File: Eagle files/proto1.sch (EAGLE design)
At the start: 10 parts, among them U1 RASPBERRY_PICOTH, U2 GY-521MPU6050, U3 HMC5883LGY-271, U4 ESP8266_ESP-01

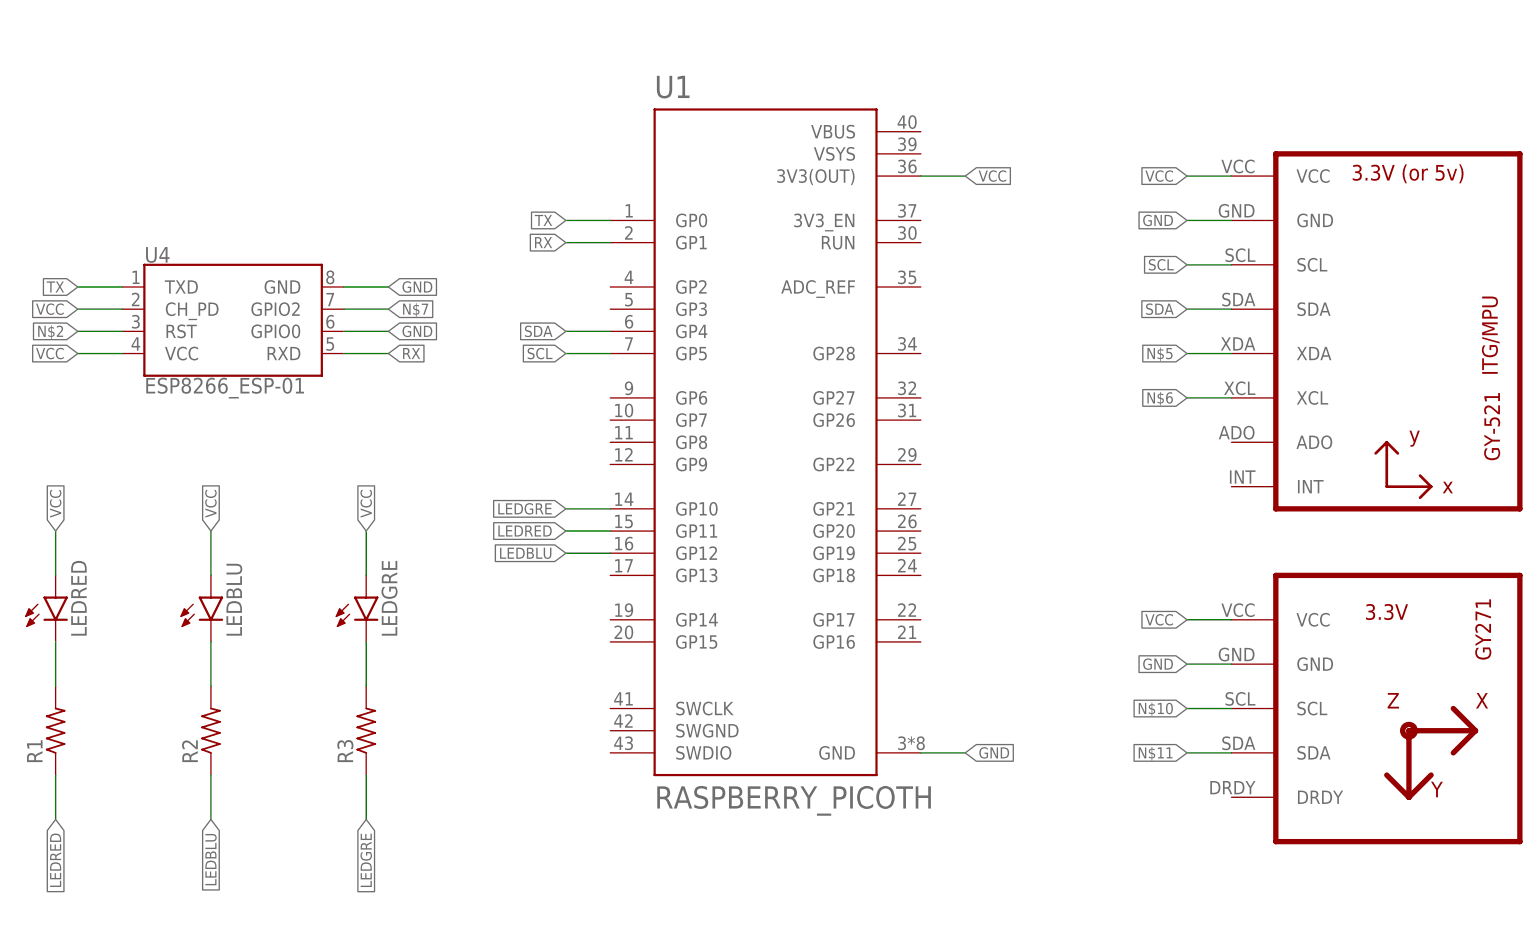
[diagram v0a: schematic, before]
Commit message: Change microcontroller
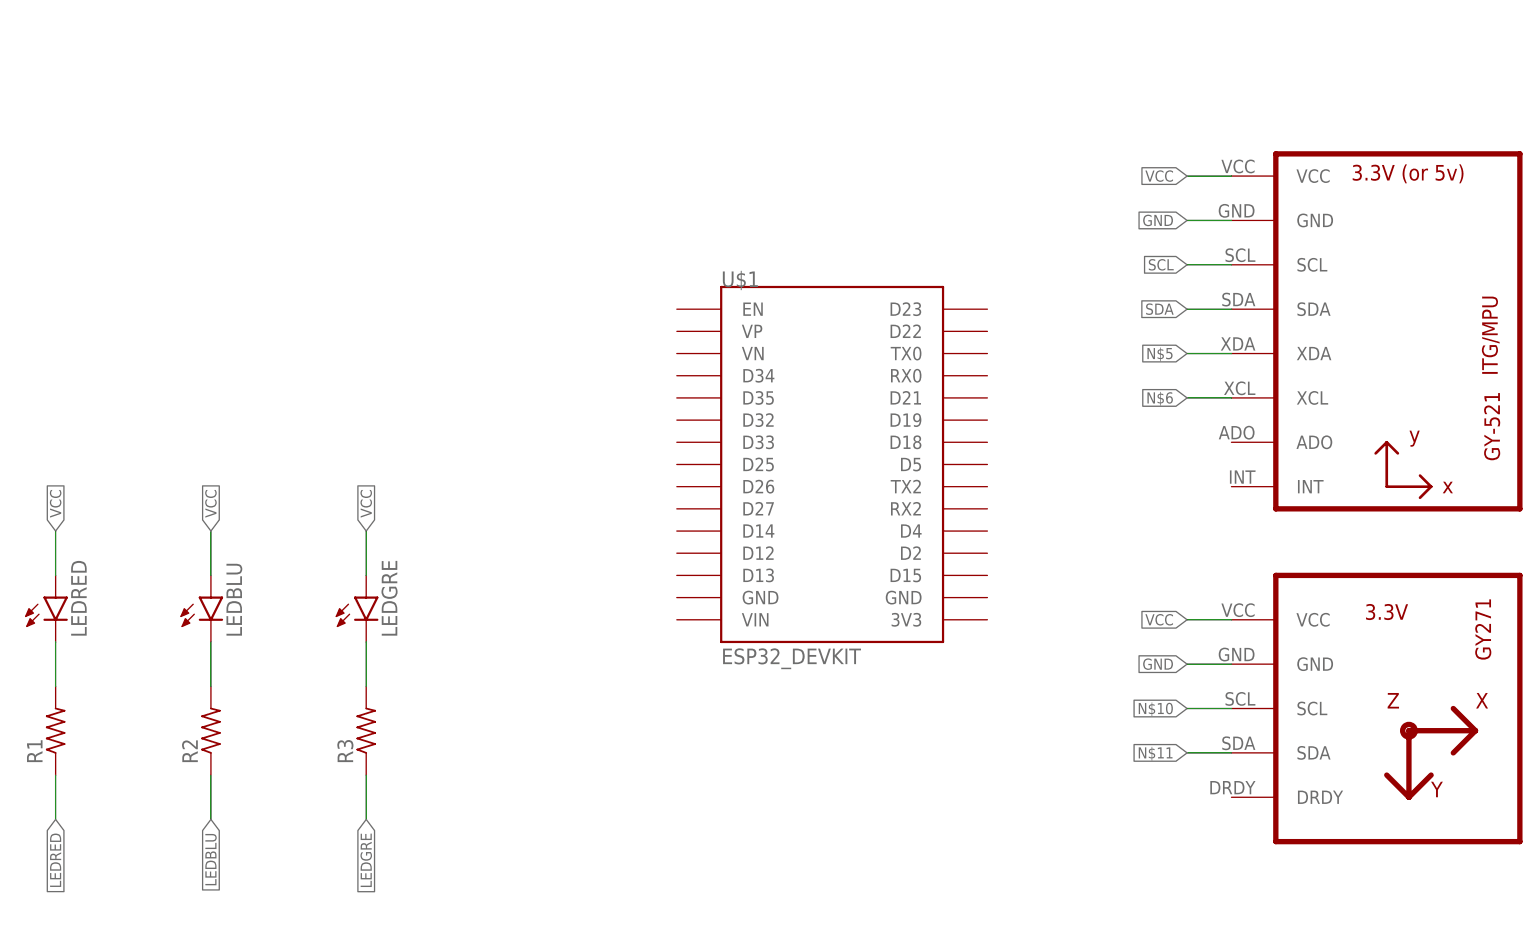
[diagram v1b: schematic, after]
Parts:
- removed U1: RASPBERRY_PICOTH, RpiPico:RASPBERRY_PICOTH
- removed U4: ESP8266_ESP-01, SparkFun-RF:ESP8266_ESP-01
- added U$1: ESP32_DEVKIT, DOIT_ESP32_DEVKIT:ESP32_DEVKIT
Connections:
- removed net N$2: U4.RST
- removed net N$7: U4.GPIO2
- removed net RX: U1.GP1, U4.RXD
- removed net TX: U1.GP0, U4.TXD
- net GND: no longer U1.GND, U4.GND, U4.GPIO0
- net LEDBLU: no longer U1.GP12
- net LEDGRE: no longer U1.GP10
- net LEDRED: no longer U1.GP11
- net SCL: no longer U1.GP5
- net SDA: no longer U1.GP4
- net VCC: no longer U1.3V3(OUT), U4.CH_PD, U4.VCC
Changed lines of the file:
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@@
 </classes>
 <parts>
-<part name="U1" library="RpiPico" deviceset="RASPBERRY_PICO" device="TH"/>
 <part name="U2" library="gy-521" deviceset="GY-521" device="MPU6050"/>
 <part name="U3" library="hmc5883l" deviceset="HMC5883L" device="GY-271"/>
-<part name="U4" library="SparkFun-RF" deviceset="ESP8266_ESP-01" device=""/>
 <part name="LEDBLU" library="led" library_urn="urn:adsk.eagle:library:259" deviceset="LED" device="5MM" package3d_urn="urn:adsk.eagle:package:15799/2"/>
 <part name="LEDGRE" library="led" library_urn="urn:adsk.eagle:library:259" deviceset="LED" device="5MM" package3d_urn="urn:adsk.eagle:package:15799/2"/>
@@
 <part name="R2" library="adafruit" deviceset="R-US_" device="0207/10"/>
 <part name="R3" library="adafruit" deviceset="R-US_" device="0207/10"/>
+<part name="U$1" library="DOIT_ESP32_DEVKIT" deviceset="ESP32_DEVKIT" device=""/>
 </parts>
 <sheets>
@@
 </plain>
 <instances>
-<instance part="U1" gate="U$1" x="86.36" y="60.96" smashed="yes">
-<attribute name="NAME" x="73.6445" y="100.3746" size="2.54388125" layer="95"/>
-<attribute name="VALUE" x="73.6531" y="19.0286" size="2.54171875" layer="96"/>
-</instance>
 <instance part="U2" gate="G$1" x="154.94" y="76.2" smashed="yes"/>
 <instance part="U3" gate="G$1" x="154.94" y="30.48" smashed="yes"/>
-<instance part="U4" gate="G$1" x="25.4" y="73.66" smashed="yes">
-<attribute name="NAME" x="15.24" y="81.534" size="1.778" layer="95"/>
-<attribute name="VALUE" x="15.24" y="68.326" size="1.778" layer="96" rot="MR180"/>
-</instance>
 <instance part="LEDBLU" gate="G$1" x="22.86" y="43.18" smashed="yes">
 <attribute name="NAME" x="26.416" y="38.608" size="1.778" layer="95" rot="R90"/>
@@
 <attribute name="VALUE" x="43.942" y="24.13" size="1.778" layer="96" rot="R90"/>
 </instance>
+<instance part="U$1" gate="G$1" x="93.98" y="58.42" smashed="yes">
+<attribute name="NAME" x="81.28" y="78.74" size="1.778" layer="95"/>
+<attribute name="VALUE" x="81.28" y="35.56" size="1.778" layer="96"/>
+</instance>
 </instances>
 <busses>
@@
 <label x="134.62" y="35.56" size="1.27" layer="95" rot="R180" xref="yes"/>
 </segment>
-<segment>
-<pinref part="U1" gate="U$1" pin="GND"/>
-<wire x1="104.14" y1="25.4" x2="109.22" y2="25.4" width="0.1524" layer="91"/>
-<label x="109.22" y="25.4" size="1.27" layer="95" xref="yes"/>
-</segment>
-<segment>
-<pinref part="U4" gate="G$1" pin="GND"/>
-<wire x1="38.1" y1="78.74" x2="43.18" y2="78.74" width="0.1524" layer="91"/>
-<label x="43.18" y="78.74" size="1.27" layer="95" xref="yes"/>
-</segment>
-<segment>
-<pinref part="U4" gate="G$1" pin="GPIO0"/>
-<wire x1="38.1" y1="73.66" x2="43.18" y2="73.66" width="0.1524" layer="91"/>
-<label x="43.18" y="73.66" size="1.27" layer="95" xref="yes"/>
-</segment>
 </net>
 <net name="SCL" class="0">
@@
 <label x="134.62" y="81.28" size="1.27" layer="95" rot="R180" xref="yes"/>
 </segment>
-<segment>
-<pinref part="U1" gate="U$1" pin="GP5"/>
-<wire x1="68.58" y1="71.12" x2="63.5" y2="71.12" width="0.1524" layer="91"/>
-<label x="63.5" y="71.12" size="1.27" layer="95" rot="R180" xref="yes"/>
-</segment>
 </net>
 <net name="SDA" class="0">
@@
 <wire x1="139.7" y1="76.2" x2="134.62" y2="76.2" width="0.1524" layer="91"/>
 <label x="134.62" y="76.2" size="1.27" layer="95" rot="R180" xref="yes"/>
-</segment>
-<segment>
-<pinref part="U1" gate="U$1" pin="GP4"/>
-<wire x1="68.58" y1="73.66" x2="63.5" y2="73.66" width="0.1524" layer="91"/>
-<label x="63.5" y="73.66" size="1.27" layer="95" rot="R180" xref="yes"/>
 </segment>
 </net>
@@
 <net name="VCC" class="0">
 <segment>
-<pinref part="U1" gate="U$1" pin="3V3(OUT)"/>
-<wire x1="104.14" y1="91.44" x2="109.22" y2="91.44" width="0.1524" layer="91"/>
-<label x="109.22" y="91.44" size="1.27" layer="95" xref="yes"/>
-</segment>
-<segment>
 <pinref part="U2" gate="G$1" pin="VCC"/>
 <wire x1="139.7" y1="91.44" x2="134.62" y2="91.44" width="0.1524" layer="91"/>
@@
 <wire x1="139.7" y1="40.64" x2="134.62" y2="40.64" width="0.1524" layer="91"/>
 <label x="134.62" y="40.64" size="1.27" layer="95" rot="R180" xref="yes"/>
-</segment>
-<segment>
-<pinref part="U4" gate="G$1" pin="VCC"/>
-<wire x1="12.7" y1="71.12" x2="7.62" y2="71.12" width="0.1524" layer="91"/>
-<label x="7.62" y="71.12" size="1.27" layer="95" rot="R180" xref="yes"/>
-</segment>
-<segment>
-<pinref part="U4" gate="G$1" pin="CH_PD"/>
-<wire x1="12.7" y1="76.2" x2="7.62" y2="76.2" width="0.1524" layer="91"/>
-<label x="7.62" y="76.2" size="1.27" layer="95" rot="R180" xref="yes"/>
 </segment>
 <segment>
@@
 </segment>
 </net>
-<net name="N$2" class="0">
-<segment>
-<pinref part="U4" gate="G$1" pin="RST"/>
-<wire x1="12.7" y1="73.66" x2="7.62" y2="73.66" width="0.1524" layer="91"/>
-<label x="7.62" y="73.66" size="1.27" layer="95" rot="R180" xref="yes"/>
-</segment>
-</net>
-<net name="N$7" class="0">
-<segment>
-<pinref part="U4" gate="G$1" pin="GPIO2"/>
-<wire x1="38.1" y1="76.2" x2="43.18" y2="76.2" width="0.1524" layer="91"/>
-<label x="43.18" y="76.2" size="1.27" layer="95" xref="yes"/>
-</segment>
-</net>
-<net name="TX" class="0">
-<segment>
-<pinref part="U1" gate="U$1" pin="GP0"/>
-<wire x1="68.58" y1="86.36" x2="63.5" y2="86.36" width="0.1524" layer="91"/>
-<label x="63.5" y="86.36" size="1.27" layer="95" rot="R180" xref="yes"/>
-</segment>
-<segment>
-<pinref part="U4" gate="G$1" pin="TXD"/>
-<wire x1="12.7" y1="78.74" x2="7.62" y2="78.74" width="0.1524" layer="91"/>
-<label x="7.62" y="78.74" size="1.27" layer="95" rot="R180" xref="yes"/>
-</segment>
-</net>
-<net name="RX" class="0">
-<segment>
-<pinref part="U1" gate="U$1" pin="GP1"/>
-<wire x1="68.58" y1="83.82" x2="63.5" y2="83.82" width="0.1524" layer="91"/>
-<label x="63.5" y="83.82" size="1.27" layer="95" rot="R180" xref="yes"/>
-</segment>
-<segment>
-<pinref part="U4" gate="G$1" pin="RXD"/>
-<wire x1="38.1" y1="71.12" x2="43.18" y2="71.12" width="0.1524" layer="91"/>
-<label x="43.18" y="71.12" size="1.27" layer="95" xref="yes"/>
-</segment>
-</net>
 <net name="LEDGRE" class="0">
-<segment>
-<pinref part="U1" gate="U$1" pin="GP10"/>
-<wire x1="68.58" y1="53.34" x2="63.5" y2="53.34" width="0.1524" layer="91"/>
-<label x="63.5" y="53.34" size="1.27" layer="95" rot="R180" xref="yes"/>
-</segment>
 <segment>
 <pinref part="R3" gate="G$1" pin="1"/>
@@
 <net name="LEDRED" class="0">
 <segment>
-<pinref part="U1" gate="U$1" pin="GP11"/>
-<wire x1="68.58" y1="50.8" x2="63.5" y2="50.8" width="0.1524" layer="91"/>
-<label x="63.5" y="50.8" size="1.27" layer="95" rot="R180" xref="yes"/>
-</segment>
-<segment>
 <pinref part="R1" gate="G$1" pin="1"/>
 <wire x1="5.08" y1="22.86" x2="5.08" y2="17.78" width="0.1524" layer="91"/>
@@
 <net name="LEDBLU" class="0">
 <segment>
-<pinref part="U1" gate="U$1" pin="GP12"/>
-<wire x1="68.58" y1="48.26" x2="63.5" y2="48.26" width="0.1524" layer="91"/>
-<label x="63.5" y="48.26" size="1.27" layer="95" rot="R180" xref="yes"/>
-</segment>
-<segment>
 <pinref part="R2" gate="G$1" pin="1"/>

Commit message: Add nets
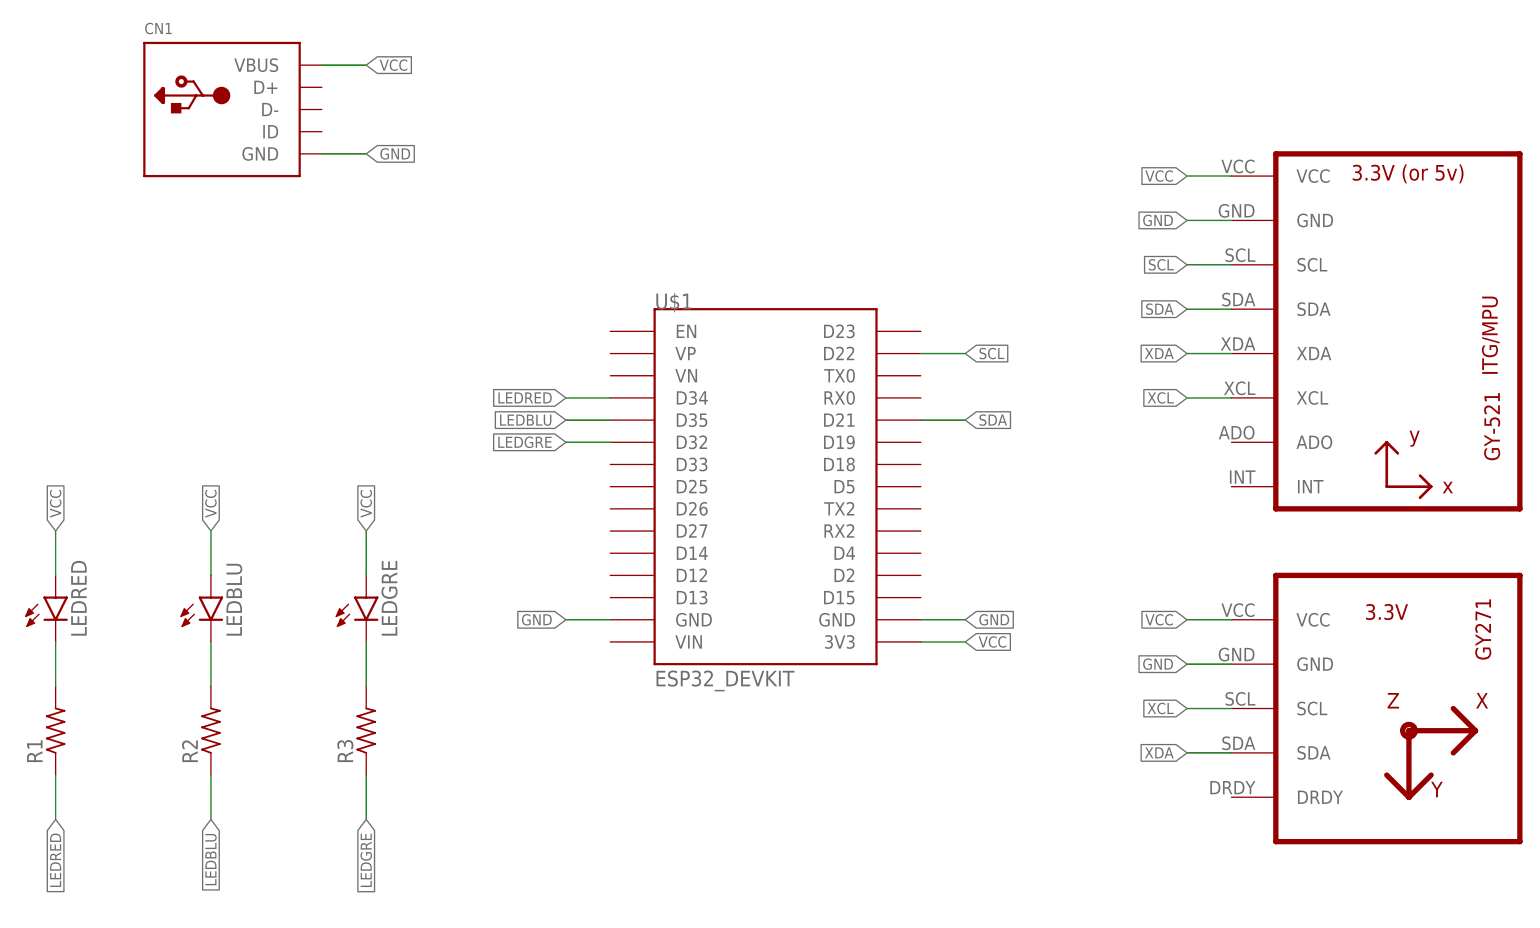
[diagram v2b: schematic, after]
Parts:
- added CN1: (no value), adafruit:USBTHM
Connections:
- removed net N$10: U3.SCL
- removed net N$11: U3.SDA
- removed net N$5: U2.XDA
- removed net N$6: U2.XCL
- new net XCL: U2.XCL, U3.SCL
- new net XDA: U2.XDA, U3.SDA
- net GND: now also CN1.GND, U$1.GND@1, U$1.GND@2
- net LEDBLU: now also U$1.D35
- net LEDGRE: now also U$1.D32
- net LEDRED: now also U$1.D34
- net SCL: now also U$1.D22
- net SDA: now also U$1.D21
- net VCC: now also CN1.VBUS, U$1.3V3
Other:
- moved on the sheet: U$1
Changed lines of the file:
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@@
 <part name="R3" library="adafruit" deviceset="R-US_" device="0207/10"/>
 <part name="U$1" library="DOIT_ESP32_DEVKIT" deviceset="ESP32_DEVKIT" device=""/>
+<part name="CN1" library="adafruit" deviceset="USB" device="THM"/>
 </parts>
 <sheets>
@@
 <attribute name="VALUE" x="43.942" y="24.13" size="1.778" layer="96" rot="R90"/>
 </instance>
-<instance part="U$1" gate="G$1" x="93.98" y="58.42" smashed="yes">
-<attribute name="NAME" x="81.28" y="78.74" size="1.778" layer="95"/>
-<attribute name="VALUE" x="81.28" y="35.56" size="1.778" layer="96"/>
+<instance part="U$1" gate="G$1" x="86.36" y="55.88" smashed="yes">
+<attribute name="NAME" x="73.66" y="76.2" size="1.778" layer="95"/>
+<attribute name="VALUE" x="73.66" y="33.02" size="1.778" layer="96"/>
+</instance>
+<instance part="CN1" gate="G$1" x="25.4" y="99.06" smashed="yes">
+<attribute name="NAME" x="15.24" y="107.696" size="1.27" layer="95"/>
+<attribute name="VALUE" x="15.24" y="88.9" size="1.27" layer="96"/>
 </instance>
 </instances>
@@
 <label x="134.62" y="35.56" size="1.27" layer="95" rot="R180" xref="yes"/>
 </segment>
+<segment>
+<pinref part="U$1" gate="G$1" pin="GND@1"/>
+<wire x1="68.58" y1="40.64" x2="63.5" y2="40.64" width="0.1524" layer="91"/>
+<label x="63.5" y="40.64" size="1.27" layer="95" rot="R180" xref="yes"/>
+</segment>
+<segment>
+<pinref part="U$1" gate="G$1" pin="GND@2"/>
+<wire x1="104.14" y1="40.64" x2="109.22" y2="40.64" width="0.1524" layer="91"/>
+<label x="109.22" y="40.64" size="1.27" layer="95" xref="yes"/>
+</segment>
+<segment>
+<pinref part="CN1" gate="G$1" pin="GND"/>
+<wire x1="35.56" y1="93.98" x2="40.64" y2="93.98" width="0.1524" layer="91"/>
+<label x="40.64" y="93.98" size="1.27" layer="95" xref="yes"/>
+</segment>
 </net>
 <net name="SCL" class="0">
@@
 <wire x1="139.7" y1="81.28" x2="134.62" y2="81.28" width="0.1524" layer="91"/>
 <label x="134.62" y="81.28" size="1.27" layer="95" rot="R180" xref="yes"/>
+</segment>
+<segment>
+<pinref part="U$1" gate="G$1" pin="D22"/>
+<wire x1="104.14" y1="71.12" x2="109.22" y2="71.12" width="0.1524" layer="91"/>
+<label x="109.22" y="71.12" size="1.27" layer="95" xref="yes"/>
 </segment>
 </net>
@@
 <label x="134.62" y="76.2" size="1.27" layer="95" rot="R180" xref="yes"/>
 </segment>
+<segment>
+<pinref part="U$1" gate="G$1" pin="D21"/>
+<wire x1="104.14" y1="63.5" x2="109.22" y2="63.5" width="0.1524" layer="91"/>
+<label x="109.22" y="63.5" size="1.27" layer="95" xref="yes"/>
+</segment>
 </net>
-<net name="N$5" class="0">
+<net name="XDA" class="0">
 <segment>
 <pinref part="U2" gate="G$1" pin="XDA"/>
@@
 <label x="134.62" y="71.12" size="1.27" layer="95" rot="R180" xref="yes"/>
 </segment>
+<segment>
+<pinref part="U3" gate="G$1" pin="SDA"/>
+<wire x1="139.7" y1="25.4" x2="134.62" y2="25.4" width="0.1524" layer="91"/>
+<label x="134.62" y="25.4" size="1.27" layer="95" rot="R180" xref="yes"/>
+</segment>
 </net>
-<net name="N$6" class="0">
+<net name="XCL" class="0">
 <segment>
 <pinref part="U2" gate="G$1" pin="XCL"/>
 <wire x1="139.7" y1="66.04" x2="134.62" y2="66.04" width="0.1524" layer="91"/>
 <label x="134.62" y="66.04" size="1.27" layer="95" rot="R180" xref="yes"/>
+</segment>
+<segment>
+<pinref part="U3" gate="G$1" pin="SCL"/>
+<wire x1="139.7" y1="30.48" x2="134.62" y2="30.48" width="0.1524" layer="91"/>
+<label x="134.62" y="30.48" size="1.27" layer="95" rot="R180" xref="yes"/>
 </segment>
 </net>
@@
 <label x="40.64" y="50.8" size="1.27" layer="95" rot="R90" xref="yes"/>
 </segment>
-</net>
-<net name="N$10" class="0">
 <segment>
-<pinref part="U3" gate="G$1" pin="SCL"/>
-<wire x1="139.7" y1="30.48" x2="134.62" y2="30.48" width="0.1524" layer="91"/>
-<label x="134.62" y="30.48" size="1.27" layer="95" rot="R180" xref="yes"/>
+<pinref part="U$1" gate="G$1" pin="3V3"/>
+<wire x1="104.14" y1="38.1" x2="109.22" y2="38.1" width="0.1524" layer="91"/>
+<label x="109.22" y="38.1" size="1.27" layer="95" xref="yes"/>
 </segment>
-</net>
-<net name="N$11" class="0">
 <segment>
-<pinref part="U3" gate="G$1" pin="SDA"/>
-<wire x1="139.7" y1="25.4" x2="134.62" y2="25.4" width="0.1524" layer="91"/>
-<label x="134.62" y="25.4" size="1.27" layer="95" rot="R180" xref="yes"/>
+<pinref part="CN1" gate="G$1" pin="VBUS"/>
+<wire x1="35.56" y1="104.14" x2="40.64" y2="104.14" width="0.1524" layer="91"/>
+<label x="40.64" y="104.14" size="1.27" layer="95" xref="yes"/>
 </segment>
 </net>
@@
 <label x="40.64" y="17.78" size="1.27" layer="95" rot="R270" xref="yes"/>
 </segment>
+<segment>
+<pinref part="U$1" gate="G$1" pin="D32"/>
+<wire x1="68.58" y1="60.96" x2="63.5" y2="60.96" width="0.1524" layer="91"/>
+<label x="63.5" y="60.96" size="1.27" layer="95" rot="R180" xref="yes"/>
+</segment>
 </net>
 <net name="LEDRED" class="0">
@@
 <wire x1="5.08" y1="22.86" x2="5.08" y2="17.78" width="0.1524" layer="91"/>
 <label x="5.08" y="17.78" size="1.27" layer="95" rot="R270" xref="yes"/>
+</segment>
+<segment>
+<pinref part="U$1" gate="G$1" pin="D34"/>
+<wire x1="68.58" y1="66.04" x2="63.5" y2="66.04" width="0.1524" layer="91"/>
+<label x="63.5" y="66.04" size="1.27" layer="95" rot="R180" xref="yes"/>
 </segment>
 </net>
@@
 <label x="22.86" y="17.78" size="1.27" layer="95" rot="R270" xref="yes"/>
 </segment>
+<segment>
+<pinref part="U$1" gate="G$1" pin="D35"/>
+<wire x1="68.58" y1="63.5" x2="63.5" y2="63.5" width="0.1524" layer="91"/>
+<label x="63.5" y="63.5" size="1.27" layer="95" rot="R180" xref="yes"/>
+</segment>
 </net>
